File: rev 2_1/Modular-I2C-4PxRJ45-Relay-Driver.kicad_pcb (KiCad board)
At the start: 2 copper layers, 69.5 x 100 mm, 123 parts, among them J1 Conn_02x03_Odd_Even, J2 Conn_02x03_Odd_Even, J3 Screw_Terminal_01x02, J4 Screw_Terminal_01x02, Q51 2N7002, Q52 2N7002, Q53 2N7002, Q54 2N7002, Q55 2N7002, Q56 2N7002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

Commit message: production files
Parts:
- removed RJ45-1: R-RJ45R04P-4000, Vizista:CONN-TH_DS1129-02-S80BP
- added J11: Screw_Terminal_01x08, VizistaHA:CONN-TH_4P-P3.50_JILN_JL15EDGRHC-35004B02, F.Cu at (126.7, 110.7)
- added J12: Screw_Terminal_01x08, VizistaHA:CONN-TH_4P-P3.50_JILN_JL15EDGRHC-35004B02, F.Cu at (142.1, 110.7)
- added J13: Screw_Terminal_01x08, VizistaHA:CONN-TH_4P-P3.50_JILN_JL15EDGRHC-35004B02, F.Cu at (157.5, 110.8)
- added J14: Screw_Terminal_01x08, VizistaHA:CONN-TH_4P-P3.50_JILN_JL15EDGRHC-35004B02, F.Cu at (172.9, 110.8)
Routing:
- net RC9-: track 15.1 -> 23.9 mm
- net RC7-: track 14.9 -> 23.6 mm
- net RC4-: track 15.8 -> 24.4 mm
- net RC6-: track 15.8 -> 24.1 mm
- net RC3-: track 16.6 -> 24.8 mm
- net RC8-: track 15.2 -> 23.4 mm
- net RC10-: track 15.2 -> 23.4 mm
- net RC13-: track 15.9 -> 23.6 mm
- net RC5-: track 17.3 -> 24.6 mm
- net RC2-: track 18.1 -> 24.8 mm
- net RC11-: track 17.0 -> 23.5 mm
- net RC14-: track 17.6 -> 24.0 mm
- net RC12-: track 17.6 -> 23.8 mm
- net RC1-: track 19.3 -> 25.1 mm
- net RC15-: track 18.9 -> 24.4 mm
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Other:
- board text added: "A 1 3 5 7 2 4 6 8"
- board text removed: "A 1 2 3 4 5 6 7 8"

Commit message: images and fabrication files
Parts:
- added G***: LOGO, Vizista_Logo:Vizista-Logo-Text-10mm, F.Cu at (162.7, 34.8)
- added G***: LOGO, Vizista_Logo:Vizista-Logo-Text-20mm, B.Cu at (166.5, 38.6)
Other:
- board text added: "Based on design by Jon Oxer by Austin's Creations"
- board text added: "Passive POE Injector v0.1 2023"
- board text removed: "Based on design by Jon Oxer by Austin's Creations modified by Mattar"

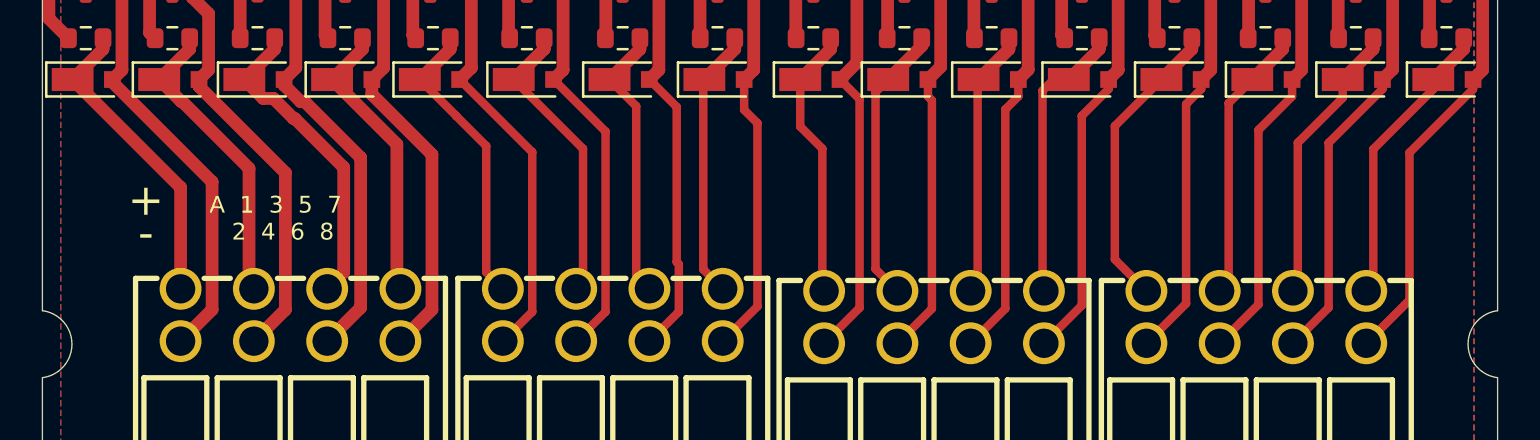
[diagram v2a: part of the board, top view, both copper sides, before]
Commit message: read me update and label
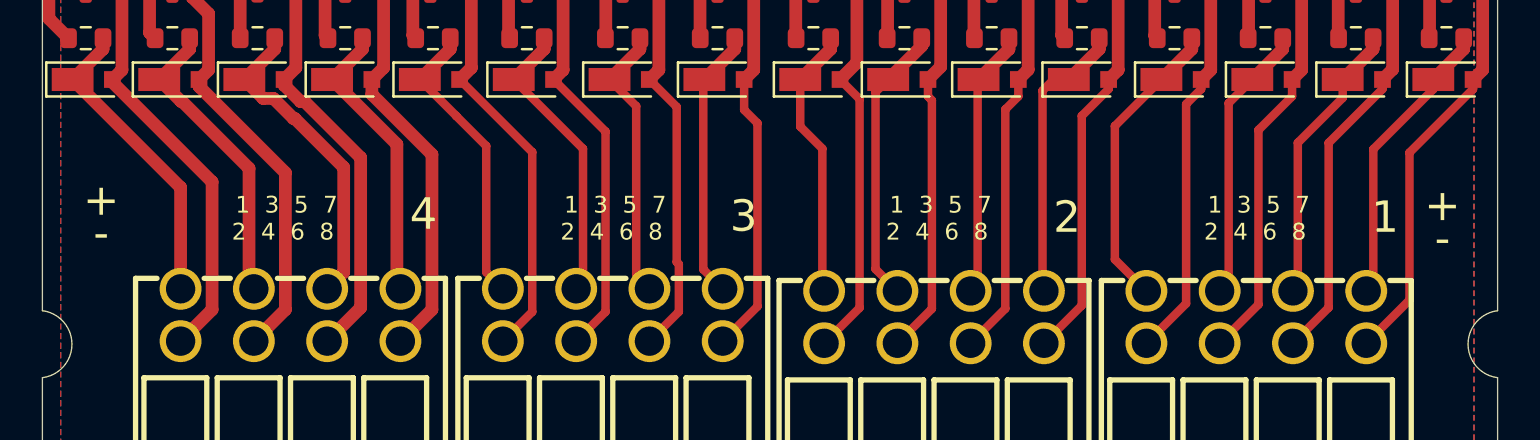
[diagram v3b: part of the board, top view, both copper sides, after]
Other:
- board text added: "1 3 5 7 2 4 6 8"
- board text added: "3"
- board text added: "4"
- board text removed: "A 1 3 5 7 2 4 6 8"
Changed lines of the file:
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@@
     (effects (font (size 0.8 0.8) (thickness 0.2)) (justify mirror))
   )
-  (gr_text "A  1  3  5  7 \n  2  4  6  8" (at 126.0348 106.0704) (layer "F.SilkS")
+  (gr_text "   1  3  5  7 \n  2  4  6  8" (at 126.0348 106.0704) (layer "F.SilkS")
     (effects (font (size 0.8 0.8) (thickness 0.2)))
   )
   (gr_text "RST" (at 118.745 33.147) (layer "F.SilkS")
     (effects (font (size 1 1) (thickness 0.125)))
+  )
+  (gr_text "   1  3  5  7 \n  2  4  6  8" (at 141.732 106.0704) (layer "F.SilkS")
+    (effects (font (size 0.8 0.8) (thickness 0.2)))
+  )
+  (gr_text "   1  3  5  7 \n  2  4  6  8" (at 172.466 106.0704) (layer "F.SilkS")
+    (effects (font (size 0.8 0.8) (thickness 0.2)))
   )
   (gr_text "2" (at 148.4376 31.242) (layer "F.SilkS")
@@
   (gr_text "1" (at 118.618 27.9028) (layer "F.SilkS")
     (effects (font (size 1 1) (thickness 0.125)))
+  )
+  (gr_text "   1  3  5  7 \n  2  4  6  8" (at 157.2768 106.0704) (layer "F.SilkS")
+    (effects (font (size 0.8 0.8) (thickness 0.2)))
+  )
+  (gr_text "+" (at 181.7624 105.4608) (layer "F.SilkS")
+    (effects (font (size 1.5 1.5) (thickness 0.3)))
   )
   (gr_text "GND" (at 173.492047 78.239153 270) (layer "F.SilkS")
@@
     (effects (font (size 1 1) (thickness 0.15)))
   )
+  (gr_text "3" (at 148.3868 105.9688) (layer "F.SilkS")
+    (effects (font (size 1.5 1.5) (thickness 0.3)))
+  )
+  (gr_text "1" (at 179.0192 106.0196) (layer "F.SilkS")
+    (effects (font (size 1.5 1.5) (thickness 0.3)))
+  )
   (gr_text "VIN\n12v" (at 172.742047 83.239153 270) (layer "F.SilkS")
     (effects (font (size 1 1) (thickness 0.15)))
+  )
+  (gr_text "-" (at 181.7624 107.0356) (layer "F.SilkS")
+    (effects (font (size 1.5 1.5) (thickness 0.3)))
   )
   (gr_text "VIN\n12v" (at 126.4949 77.8144 90) (layer "F.SilkS")
@@
   (gr_text "0" (at 146.70835 25.5028) (layer "F.SilkS")
     (effects (font (size 1 1) (thickness 0.125)))
+  )
+  (gr_text "4" (at 133.096 105.8672) (layer "F.SilkS")
+    (effects (font (size 1.5 1.5) (thickness 0.3)))
   )
   (gr_text "2" (at 118.491 30.4028) (layer "F.SilkS")
@@
     (effects (font (size 1 1) (thickness 0.125)))
   )
-  (gr_text "+" (at 119.8372 105.2068) (layer "F.SilkS")
+  (gr_text "+" (at 117.7036 105.2068) (layer "F.SilkS")
     (effects (font (size 1.5 1.5) (thickness 0.3)))
   )
-  (gr_text "-" (at 119.8372 106.7816) (layer "F.SilkS")
+  (gr_text "2" (at 163.83 106.0196) (layer "F.SilkS")
     (effects (font (size 1.5 1.5) (thickness 0.3)))
   )
+  (gr_text "-" (at 117.7036 106.7816) (layer "F.SilkS")
+    (effects (font (size 1.5 1.5) (thickness 0.3)))
+  )

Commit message: cleanup
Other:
- board text removed: "1: Data 1 2: Data 2 3: Data 3 4: VIN 5: VIN 6: Data 4 7: GND 8: GND"
- board text removed: "Copyright 2019-2021 SuperHouse Automation Pty Ltd Released under the terms of the TAPR Open Hardware License: www.tapr.org/OHL"
- board text removed: "Passive POE Injector v0.1 2023"
- board text removed: "RJ45 Pinout"
- board text removed: "www.superhouse.tv/i2crj45"
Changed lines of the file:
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@@
       ) (layer "B.SilkS") (width 0) (fill solid))
   )
-  (gr_line (start 348.456014 74.534986) (end 348.456014 89.534986) (layer "B.SilkS") (width 0.254))
-  (gr_arc (start 348.456014 89.534986) (mid 347.870233 90.949214) (end 346.456014 91.534986) (layer "B.SilkS") (width 0.254))
-  (gr_arc (start 333.956014 91.534986) (mid 332.541796 90.949204) (end 331.956014 89.534986) (layer "B.SilkS") (width 0.254))
   (gr_line (start 173.688351 56.1308) (end 170.894351 54.3528) (layer "B.SilkS") (width 0.254))
   (gr_line (start 173.180351 55.8768) (end 172.926351 55.8768) (layer "B.SilkS") (width 0.254))
   (gr_line (start 169.116351 55.8768) (end 170.894351 54.6068) (layer "B.SilkS") (width 0.254))
-  (gr_arc (start 346.456014 72.534986) (mid 347.870223 73.120777) (end 348.456014 74.534986) (layer "B.SilkS") (width 0.254))
   (gr_line (start 168.354351 56.1308) (end 173.688351 56.1308) (layer "B.SilkS") (width 0.254))
   (gr_line (start 170.132351 55.3688) (end 171.402351 55.3688) (layer "B.SilkS") (width 0.4064))
   (gr_line (start 170.894351 54.3528) (end 168.354351 56.1308) (layer "B.SilkS") (width 0.254))
   (gr_line (start 171.402351 55.3688) (end 170.894351 55.1148) (layer "B.SilkS") (width 0.4064))
-  (gr_arc (start 331.956014 74.534986) (mid 332.541806 73.120786) (end 333.956014 72.534986) (layer "B.SilkS") (width 0.254))
-  (gr_line (start 346.451014 91.559986) (end 333.951014 91.559986) (layer "B.SilkS") (width 0.254))
   (gr_line (start 172.418351 55.6228) (end 170.894351 54.8608) (layer "B.SilkS") (width 0.4064))
   (gr_line (start 170.894351 54.6068) (end 172.926351 55.8768) (layer "B.SilkS") (width 0.254))
   (gr_line (start 172.926351 55.8768) (end 169.116351 55.8768) (layer "B.SilkS") (width 0.254))
   (gr_line (start 170.894351 54.8608) (end 170.132351 55.3688) (layer "B.SilkS") (width 0.4064))
-  (gr_line (start 333.956014 72.534986) (end 346.456014 72.534986) (layer "B.SilkS") (width 0.254))
   (gr_line (start 169.624351 55.6228) (end 172.418351 55.6228) (layer "B.SilkS") (width 0.4064))
   (gr_arc (start 126.7449 83.8794) (mid 126.598453 84.232953) (end 126.2449 84.3794) (layer "F.SilkS") (width 0.15))
@@
   (gr_circle (center 114.711 28.077) (end 117.861 28.077) (layer "User.9") (width 0.05) (fill none))
   (gr_circle (center 114.701 112.077) (end 117.851 112.077) (layer "User.9") (width 0.05) (fill none))
-  (gr_text "www.superhouse.tv/i2crj45" (at 341.757 108.585) (layer "B.SilkS")
-    (effects (font (size 1.909 1.909) (thickness 0.391)) (justify bottom mirror))
-  )
   (gr_text "Modular\n4-Port\nI2C RJ45\nRelay Driver Breakout" (at 152.4 44.831) (layer "B.SilkS")
     (effects (font (size 2.324 2) (thickness 0.476)) (justify left bottom mirror))
@@
     (effects (font (size 0.8 0.8) (thickness 0.2)) (justify mirror))
   )
-  (gr_text "1: Data 1\n2: Data 2\n3: Data 3\n4: VIN\n5: VIN\n6: Data 4\n7: GND\n8: GND" (at 344.773014 90.797986) (layer "B.SilkS")
-    (effects (font (size 1.26 1.26) (thickness 0.24)) (justify left bottom mirror))
-  )
   (gr_text "GND" (at 116.967 52.197 270) (layer "B.SilkS")
     (effects (font (size 0.8 0.8) (thickness 0.2)) (justify mirror))
@@
   (gr_text "SDA" (at 118.967 57.097 -90) (layer "B.SilkS")
     (effects (font (size 0.8 0.8) (thickness 0.2)) (justify mirror))
-  )
-  (gr_text "RJ45 Pinout" (at 344.773014 74.414986) (layer "B.SilkS")
-    (effects (font (size 1.148 1.148) (thickness 0.252)) (justify left bottom mirror))
-  )
-  (gr_text "Copyright 2019-2021 SuperHouse Automation Pty Ltd\n\nReleased under the terms of the TAPR\nOpen Hardware License: www.tapr.org/OHL" (at 362.458 103.759) (layer "B.SilkS")
-    (effects (font (size 1.0541 1.0541) (thickness 0.2159)) (justify left bottom mirror))
   )
   (gr_text "Based on design \n by Jon Oxer\n by Austin's Creations\n" (at 152.4 52.705) (layer "B.SilkS")
@@
     (effects (font (size 1 1) (thickness 0.125)))
   )
-  (gr_text "Passive POE Injector\nv0.1 2023" (at 318.77 78.105) (layer "B.Fab")
-    (effects (font (size 2 2) (thickness 0.3)) (justify mirror))
-  )
   (dimension (type aligned) (layer "User.2")
